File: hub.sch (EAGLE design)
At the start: 7 parts, among them U1 10118194-MICRO-USB, U2 LM3671MF-3.3/NOPBMF05A-M

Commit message: Update hub.sch
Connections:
- removed net V+: F1.1
- new net N$3: C1.1, F1.2, U2.EN, U2.VIN
- net +5V: now also F1.1; no longer C1.1, F1.2, U2.EN, U2.VIN
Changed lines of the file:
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@@
 <part name="GND1" library="supply1" library_urn="urn:adsk.eagle:library:371" deviceset="GND" device=""/>
 <part name="U2" library="nebrius" deviceset="LM3671MF-3.3/NOPB" device="MF05A-M"/>
-<part name="P+2" library="supply1" library_urn="urn:adsk.eagle:library:371" deviceset="+5V" device=""/>
-<part name="P+1" library="supply1" library_urn="urn:adsk.eagle:library:371" deviceset="V+" device=""/>
 <part name="GND2" library="supply1" library_urn="urn:adsk.eagle:library:371" deviceset="GND" device=""/>
 <part name="C1" library="rcl" library_urn="urn:adsk.eagle:library:334" deviceset="C-US" device="C0805" package3d_urn="urn:adsk.eagle:package:23617/2" value="4.7uF"/>
@@
 <part name="U$3" library="nebrius" deviceset="CL-SA-12C4" device=""/>
 <part name="L1" library="nebrius" deviceset="IND-0805" device="" value="2.2uH"/>
+<part name="P+1" library="supply1" library_urn="urn:adsk.eagle:library:371" deviceset="+5V" device=""/>
 </parts>
 <sheets>
@@
 <attribute name="VALUE" x="77.1906" y="37.0586" size="2.0828" layer="96" ratio="6" rot="SR0"/>
 </instance>
-<instance part="P+2" gate="1" x="68.58" y="35.56" smashed="yes">
-<attribute name="VALUE" x="68.58" y="36.83" size="1.778" layer="96" rot="R90"/>
-</instance>
-<instance part="P+1" gate="1" x="53.34" y="35.56" smashed="yes">
-<attribute name="VALUE" x="54.61" y="36.83" size="1.778" layer="96" rot="R90"/>
-</instance>
 <instance part="GND2" gate="1" x="116.84" y="15.24" smashed="yes">
 <attribute name="VALUE" x="114.3" y="12.7" size="1.778" layer="96"/>
@@
 </instance>
 <instance part="P+3" gate="VCC" x="132.08" y="35.56" smashed="yes">
-<attribute name="VALUE" x="129.54" y="33.02" size="1.778" layer="96" rot="R90"/>
+<attribute name="VALUE" x="134.62" y="39.37" size="1.778" layer="96" rot="R180"/>
 </instance>
 <instance part="C2" gate="G$1" x="132.08" y="6.35" smashed="yes">
@@
 <attribute name="NAME" x="117.04" y="33.274" size="1.778" layer="95"/>
 <attribute name="VALUE" x="117.04" y="27.432" size="1.778" layer="96"/>
+</instance>
+<instance part="P+1" gate="1" x="53.34" y="35.56" smashed="yes">
+<attribute name="VALUE" x="54.61" y="38.1" size="1.778" layer="96" rot="R180"/>
 </instance>
 </instances>
@@
 <pinref part="GND4" gate="1" pin="GND"/>
 <wire x1="132.08" y1="1.27" x2="132.08" y2="-1.27" width="0.1524" layer="91"/>
-</segment>
-</net>
-<net name="V+" class="0">
-<segment>
-<pinref part="P+1" gate="1" pin="V+"/>
-<wire x1="53.34" y1="33.02" x2="53.34" y2="30.48" width="0.1524" layer="91"/>
-<wire x1="53.34" y1="30.48" x2="55.88" y2="30.48" width="0.1524" layer="91"/>
-<pinref part="F1" gate="A" pin="1"/>
-</segment>
-</net>
-<net name="+5V" class="0">
-<segment>
-<pinref part="P+2" gate="1" pin="+5V"/>
-<wire x1="68.58" y1="30.48" x2="68.58" y2="33.02" width="0.1524" layer="91"/>
-<pinref part="U2" gate="A" pin="VIN"/>
-<wire x1="78.74" y1="30.48" x2="76.2" y2="30.48" width="0.1524" layer="91"/>
-<junction x="68.58" y="30.48"/>
-<pinref part="U2" gate="A" pin="EN"/>
-<wire x1="76.2" y1="30.48" x2="68.58" y2="30.48" width="0.1524" layer="91"/>
-<wire x1="78.74" y1="25.4" x2="76.2" y2="25.4" width="0.1524" layer="91"/>
-<wire x1="76.2" y1="25.4" x2="76.2" y2="30.48" width="0.1524" layer="91"/>
-<junction x="76.2" y="30.48"/>
-<pinref part="C1" gate="G$1" pin="1"/>
-<wire x1="68.58" y1="30.48" x2="68.58" y2="27.94" width="0.1524" layer="91"/>
-<pinref part="F1" gate="A" pin="2"/>
-<wire x1="66.04" y1="30.48" x2="68.58" y2="30.48" width="0.1524" layer="91"/>
 </segment>
 </net>
@@
 </segment>
 </net>
+<net name="N$3" class="0">
+<segment>
+<pinref part="U2" gate="A" pin="VIN"/>
+<wire x1="78.74" y1="30.48" x2="76.2" y2="30.48" width="0.1524" layer="91"/>
+<junction x="68.58" y="30.48"/>
+<pinref part="U2" gate="A" pin="EN"/>
+<wire x1="76.2" y1="30.48" x2="68.58" y2="30.48" width="0.1524" layer="91"/>
+<wire x1="78.74" y1="25.4" x2="76.2" y2="25.4" width="0.1524" layer="91"/>
+<wire x1="76.2" y1="25.4" x2="76.2" y2="30.48" width="0.1524" layer="91"/>
+<junction x="76.2" y="30.48"/>
+<pinref part="C1" gate="G$1" pin="1"/>
+<wire x1="68.58" y1="30.48" x2="68.58" y2="27.94" width="0.1524" layer="91"/>
+<pinref part="F1" gate="A" pin="2"/>
+<wire x1="66.04" y1="30.48" x2="68.58" y2="30.48" width="0.1524" layer="91"/>
+</segment>
+</net>
+<net name="+5V" class="0">
+<segment>
+<wire x1="53.34" y1="33.02" x2="53.34" y2="30.48" width="0.1524" layer="91"/>
+<wire x1="53.34" y1="30.48" x2="55.88" y2="30.48" width="0.1524" layer="91"/>
+<pinref part="F1" gate="A" pin="1"/>
+<pinref part="P+1" gate="1" pin="+5V"/>
+</segment>
+</net>

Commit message: Lots of progress
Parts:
- added JP2: FTDI, pinhead:PINHD-1X6
- added JP4: LED, pinhead:PINHD-1X4
- added JP5: LED Type Select, pinhead:PINHD-1X3
- added U$2: ESP32-WROOM-32D, nebrius:ESP32-WROOM-32D
- added U3, U4: SN74LVC1T45DBVRDBV6-M, nebrius:SN74LVC1T45DBVRDBV6-M
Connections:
- new net LED_CLOCK: U$2.IO14, U4.B
- new net LED_DATA: U$2.IO13, U3.B
- new net N$7: JP4.2, JP5.2
- new net N$8: JP4.3, U3.A
- new net N$9: JP5.3, U4.A
- net +5V: now also JP4.1, JP5.1, U3.VCCA, U4.VCCA
- net GND: now also JP4.4, U$2.GND@1, U$2.GND@2, U$2.GND@3, U$2.GND@4, U3.DIR, U3.GND, U4.DIR, U4.GND
- net VCC: now also U$2.3V3, U3.VCCB, U4.VCCB

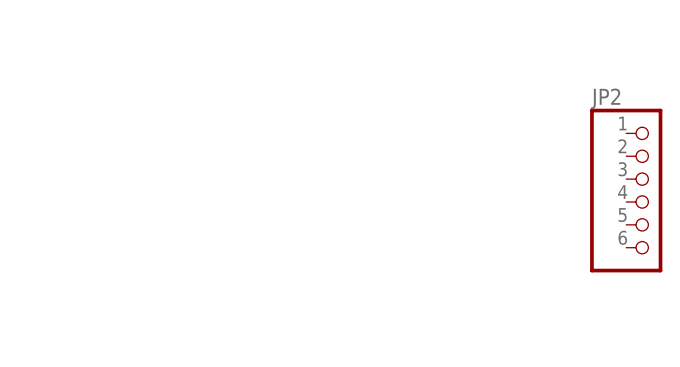
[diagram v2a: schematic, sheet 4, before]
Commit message: First draft of serial interface
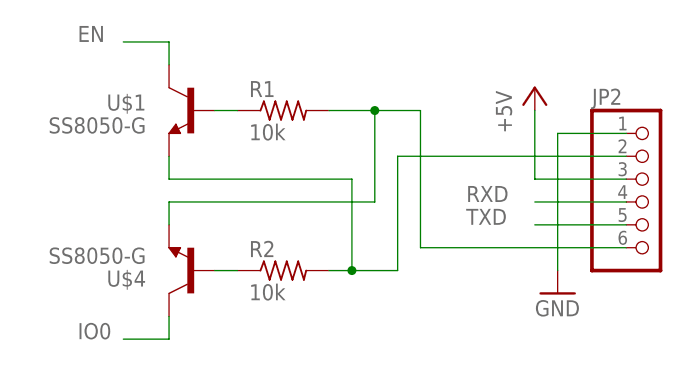
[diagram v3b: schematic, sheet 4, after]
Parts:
- added R1, R2: 10k, rcl:R-US_R0805
- added U$1, U$4: SS8050-G, nebrius:SS8050-G
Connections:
- new net EN: U$1.C
- new net IO0: U$4.C
- new net N$12: JP2.6, R1.2, U$4.E
- new net N$4: R1.1, U$1.B
- new net N$5: R2.1, U$4.B
- new net N$6: JP2.2, R2.2, U$1.E
- new net RXD: JP2.4
- new net TXD: JP2.5
- net +5V: now also JP2.3
- net GND: now also JP2.1
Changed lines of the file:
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@@
 <part name="P+9" library="supply1" library_urn="urn:adsk.eagle:library:371" deviceset="+5V" device=""/>
 <part name="P+2" library="supply1" library_urn="urn:adsk.eagle:library:371" deviceset="+5V" device=""/>
+<part name="GND14" library="supply1" library_urn="urn:adsk.eagle:library:371" deviceset="GND" device=""/>
+<part name="P+10" library="supply1" library_urn="urn:adsk.eagle:library:371" deviceset="+5V" device=""/>
+<part name="R1" library="rcl" library_urn="urn:adsk.eagle:library:334" deviceset="R-US_" device="R0805" package3d_urn="urn:adsk.eagle:package:23553/2" value="10k"/>
+<part name="R2" library="rcl" library_urn="urn:adsk.eagle:library:334" deviceset="R-US_" device="R0805" package3d_urn="urn:adsk.eagle:package:23553/2" value="10k"/>
+<part name="U$1" library="nebrius" deviceset="SS8050-G" device=""/>
+<part name="U$4" library="nebrius" deviceset="SS8050-G" device=""/>
 </parts>
 <sheets>
@@
 <attribute name="NAME" x="74.93" y="59.055" size="1.778" layer="95"/>
 </instance>
+<instance part="GND14" gate="1" x="71.12" y="38.1" smashed="yes">
+<attribute name="VALUE" x="68.58" y="35.56" size="1.778" layer="96"/>
+</instance>
+<instance part="P+10" gate="1" x="68.58" y="60.96" smashed="yes">
+<attribute name="VALUE" x="66.04" y="55.88" size="1.778" layer="96" rot="R90"/>
+</instance>
+<instance part="R1" gate="G$1" x="40.64" y="58.42" smashed="yes">
+<attribute name="NAME" x="36.83" y="59.9186" size="1.778" layer="95"/>
+<attribute name="VALUE" x="36.83" y="55.118" size="1.778" layer="96"/>
+</instance>
+<instance part="R2" gate="G$1" x="40.64" y="40.64" smashed="yes">
+<attribute name="NAME" x="36.83" y="42.1386" size="1.778" layer="95"/>
+<attribute name="VALUE" x="36.83" y="37.338" size="1.778" layer="96"/>
+</instance>
+<instance part="U$1" gate="G$1" x="30.48" y="58.42" smashed="yes" rot="MR0">
+<attribute name="NAME" x="25.4" y="58.42" size="1.778" layer="95" rot="MR0"/>
+<attribute name="VALUE" x="25.4" y="55.88" size="1.778" layer="96" rot="MR0"/>
+</instance>
+<instance part="U$4" gate="G$1" x="30.48" y="40.64" smashed="yes" rot="R180">
+<attribute name="NAME" x="25.4" y="40.64" size="1.778" layer="95" rot="R180"/>
+<attribute name="VALUE" x="25.4" y="43.18" size="1.778" layer="96" rot="R180"/>
+</instance>
 </instances>
 <busses>
 </busses>
 <nets>
+<net name="TXD" class="0">
+<segment>
+<pinref part="JP2" gate="A" pin="5"/>
+<wire x1="78.74" y1="45.72" x2="68.58" y2="45.72" width="0.1524" layer="91"/>
+<label x="60.96" y="45.72" size="1.778" layer="95"/>
+</segment>
+</net>
+<net name="RXD" class="0">
+<segment>
+<pinref part="JP2" gate="A" pin="4"/>
+<wire x1="78.74" y1="48.26" x2="68.58" y2="48.26" width="0.1524" layer="91"/>
+<label x="60.96" y="48.26" size="1.778" layer="95"/>
+</segment>
+</net>
+<net name="GND" class="0">
+<segment>
+<pinref part="JP2" gate="A" pin="1"/>
+<pinref part="GND14" gate="1" pin="GND"/>
+<wire x1="78.74" y1="55.88" x2="71.12" y2="55.88" width="0.1524" layer="91"/>
+<wire x1="71.12" y1="55.88" x2="71.12" y2="40.64" width="0.1524" layer="91"/>
+</segment>
+</net>
+<net name="+5V" class="0">
+<segment>
+<pinref part="JP2" gate="A" pin="3"/>
+<wire x1="78.74" y1="50.8" x2="68.58" y2="50.8" width="0.1524" layer="91"/>
+<pinref part="P+10" gate="1" pin="+5V"/>
+<wire x1="68.58" y1="50.8" x2="68.58" y2="58.42" width="0.1524" layer="91"/>
+</segment>
+</net>
+<net name="N$4" class="0">
+<segment>
+<pinref part="U$1" gate="G$1" pin="B"/>
+<pinref part="R1" gate="G$1" pin="1"/>
+<wire x1="33.02" y1="58.42" x2="35.56" y2="58.42" width="0.1524" layer="91"/>
+</segment>
+</net>
+<net name="N$6" class="0">
+<segment>
+<pinref part="R2" gate="G$1" pin="2"/>
+<wire x1="45.72" y1="40.64" x2="48.26" y2="40.64" width="0.1524" layer="91"/>
+<pinref part="U$1" gate="G$1" pin="E"/>
+<wire x1="27.94" y1="53.34" x2="27.94" y2="50.8" width="0.1524" layer="91"/>
+<wire x1="27.94" y1="50.8" x2="48.26" y2="50.8" width="0.1524" layer="91"/>
+<wire x1="48.26" y1="50.8" x2="48.26" y2="40.64" width="0.1524" layer="91"/>
+<junction x="48.26" y="40.64"/>
+<wire x1="48.26" y1="40.64" x2="53.34" y2="40.64" width="0.1524" layer="91"/>
+<wire x1="53.34" y1="40.64" x2="53.34" y2="53.34" width="0.1524" layer="91"/>
+<pinref part="JP2" gate="A" pin="2"/>
+<wire x1="53.34" y1="53.34" x2="78.74" y2="53.34" width="0.1524" layer="91"/>
+</segment>
+</net>
+<net name="N$12" class="0">
+<segment>
+<wire x1="27.94" y1="48.26" x2="50.8" y2="48.26" width="0.1524" layer="91"/>
+<pinref part="R1" gate="G$1" pin="2"/>
+<wire x1="45.72" y1="58.42" x2="50.8" y2="58.42" width="0.1524" layer="91"/>
+<wire x1="50.8" y1="48.26" x2="50.8" y2="58.42" width="0.1524" layer="91"/>
+<junction x="50.8" y="58.42"/>
+<pinref part="U$4" gate="G$1" pin="E"/>
+<wire x1="27.94" y1="48.26" x2="27.94" y2="45.72" width="0.1524" layer="91"/>
+<wire x1="50.8" y1="58.42" x2="55.88" y2="58.42" width="0.1524" layer="91"/>
+<wire x1="55.88" y1="58.42" x2="55.88" y2="43.18" width="0.1524" layer="91"/>
+<pinref part="JP2" gate="A" pin="6"/>
+<wire x1="55.88" y1="43.18" x2="78.74" y2="43.18" width="0.1524" layer="91"/>
+</segment>
+</net>
+<net name="N$5" class="0">
+<segment>
+<pinref part="U$4" gate="G$1" pin="B"/>
+<pinref part="R2" gate="G$1" pin="1"/>
+<wire x1="33.02" y1="40.64" x2="35.56" y2="40.64" width="0.1524" layer="91"/>
+</segment>
+</net>
+<net name="IO0" class="0">
+<segment>
+<pinref part="U$4" gate="G$1" pin="C"/>
+<wire x1="27.94" y1="35.56" x2="27.94" y2="33.02" width="0.1524" layer="91"/>
+<wire x1="27.94" y1="33.02" x2="22.86" y2="33.02" width="0.1524" layer="91"/>
+<label x="17.78" y="33.02" size="1.778" layer="95"/>
+</segment>
+</net>
+<net name="EN" class="0">
+<segment>
+<pinref part="U$1" gate="G$1" pin="C"/>
+<wire x1="27.94" y1="63.5" x2="27.94" y2="66.04" width="0.1524" layer="91"/>
+<wire x1="27.94" y1="66.04" x2="22.86" y2="66.04" width="0.1524" layer="91"/>
+<label x="17.78" y="66.04" size="1.778" layer="95"/>
+</segment>
+</net>
 </nets>
 </sheet>

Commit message: Added joystick
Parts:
- added C3: 0.1uF, rcl:C-USC0805
- added JP1: (no value), pinhead:PINHD-1X4
- added R3, R4: 10k, rcl:R-US_R0805
- added R5: 10k, nebrius:744C083
- added S1: (no value), SparkFun-Switches:JOYSTICK_MINI
- added U$7, U$8: KMR641NG, nebrius:KMR641NG
- JP4: value LED -> LED Header
- JP5: value LED Type Select -> LED Type Jumper
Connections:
- new net CENTER: R4.1, S1.CENT
- new net DOWN: R5.1, S1.DOWN
- new net LEFT: R5.3, S1.LEFT
- new net RIGHT: R5.4, S1.RIGHT
- new net SCL: JP1.4, U$2.IO21
- new net SDA: JP1.3, U$2.IO22
- new net UP: R5.2, S1.UP
- net +5V: no longer JP2.3
- net EN: now also C3.1, R3.1, U$2.EN, U$7.S
- net GND: now also C3.2, JP1.1, S1.GND, U$7.P, U$8.P
- net IO0: now also U$2.IO0, U$8.S
- net RXD: now also U$2.RXD0
- net TXD: now also U$2.TXD0
- net VCC: now also JP1.2, R3.2, R4.2, R5.5, R5.6, R5.7, R5.8

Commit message: Finished headers
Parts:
- removed C3: 0.1uF, rcl:C-USC0805
- added JP3: I2C, pinhead:PINHD-1X4
- added JP6: JTAG Enable, jumper:JP2E
- added JP7: (no value), pinhead:PINHD-2X5
- added LED1: Power, led:LEDCHIPLED_0805
- added LED2, LED3: (no value), led:LEDCHIPLED_0805
- added R6: 68, rcl:R-US_R0805
- added R7, R8: (no value), rcl:R-US_R0805
- JP1: value (none) -> JTAG; device pinhead:PINHD-1X4 -> pinhead:PINHD-1X6
- JP4: value LED Header -> LED Strip; device pinhead:PINHD-1X4 -> pinhead:PINHD-1X4/90
- JP5: value LED Type Jumper -> LED Type; device pinhead:PINHD-1X3 -> jumper:JP2E
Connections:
- new net IO16: JP7.8, U$2.IO16
- new net IO17: JP7.6, U$2.IO17
- new net IO25: JP7.2, U$2.IO25
- new net IO26: JP7.4, U$2.IO26
- new net IO34: JP7.7, U$2.IO34
- new net IO35: JP7.9, U$2.IO35
- new net IO36: JP7.3, U$2.SENSOR_VP
- new net IO39: JP7.5, U$2.SENSOR_VN
- new net N$10: LED1.C, R6.2
- new net N$11: LED2.C, R7.2
- new net N$13: LED3.C, R8.2
- new net N$14: LED3.A, U$2.IO19
- new net N$15: LED2.A, U$2.IO5
- new net TCK: JP1.4, U$2.IO13
- new net TDI: JP1.3, U$2.IO12
- new net TDO: JP1.2, U$2.IO15
- new net TMS: JP1.5, U$2.IO14
- new net TRST_N: JP1.1, JP6.1
- net +5V: no longer JP5.1
- net EN: now also JP6.2, JP6.3; no longer C3.1
- net GND: now also JP1.6, JP3.1, JP5.1, JP7.10, R6.1, R7.1, R8.1; no longer C3.2, JP1.1
- net LED_CLOCK: now also U$2.IO18; no longer U$2.IO14
- net LED_DATA: now also U$2.IO23; no longer U$2.IO13
- net N$7: now also JP4.3; no longer JP4.2
- net N$8: now also JP4.2; no longer JP4.3
- net SCL: now also JP3.4; no longer JP1.4
- net SDA: now also JP3.3; no longer JP1.3
- net VCC: now also JP3.2, JP7.1, LED1.A; no longer JP1.2

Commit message: First draft complete?
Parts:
- removed JP3: I2C, pinhead:PINHD-1X4
- removed LED2, LED3: (no value), led:LEDCHIPLED_0805
- removed R7, R8: (no value), rcl:R-US_R0805
- removed U$7, U$8: KMR641NG, nebrius:KMR641NG
- added U$5: SSD1306-OLED, nebrius:SSD1306-OLED
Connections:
- removed net IO34: JP7.7, U$2.IO34
- removed net IO35: JP7.9, U$2.IO35
- removed net IO36: JP7.3, U$2.SENSOR_VP
- removed net IO39: JP7.5, U$2.SENSOR_VN
- removed net N$11: LED2.C, R7.2
- removed net N$13: LED3.C, R8.2
- removed net N$14: LED3.A, U$2.IO19
- removed net N$15: LED2.A, U$2.IO5
- new net IO19: JP7.2, U$2.IO19
- new net IO27: JP7.9, U$2.IO27
- new net IO33: JP7.3, U$2.IO33
- new net IO4: JP7.8, U$2.IO4
- net EN: no longer U$7.S
- net GND: now also U$5.GND; no longer JP3.1, R7.1, R8.1, U$7.P, U$8.P
- net IO0: no longer U$8.S
- net IO16: now also JP7.4; no longer JP7.8
- net IO25: now also JP7.5; no longer JP7.2
- net IO26: now also JP7.7; no longer JP7.4
- net SCL: now also U$5.SCL; no longer JP3.4
- net SDA: now also U$5.SDA; no longer JP3.3
- net VCC: now also U$5.VCC; no longer JP3.2
